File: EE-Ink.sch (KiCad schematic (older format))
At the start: 14 parts

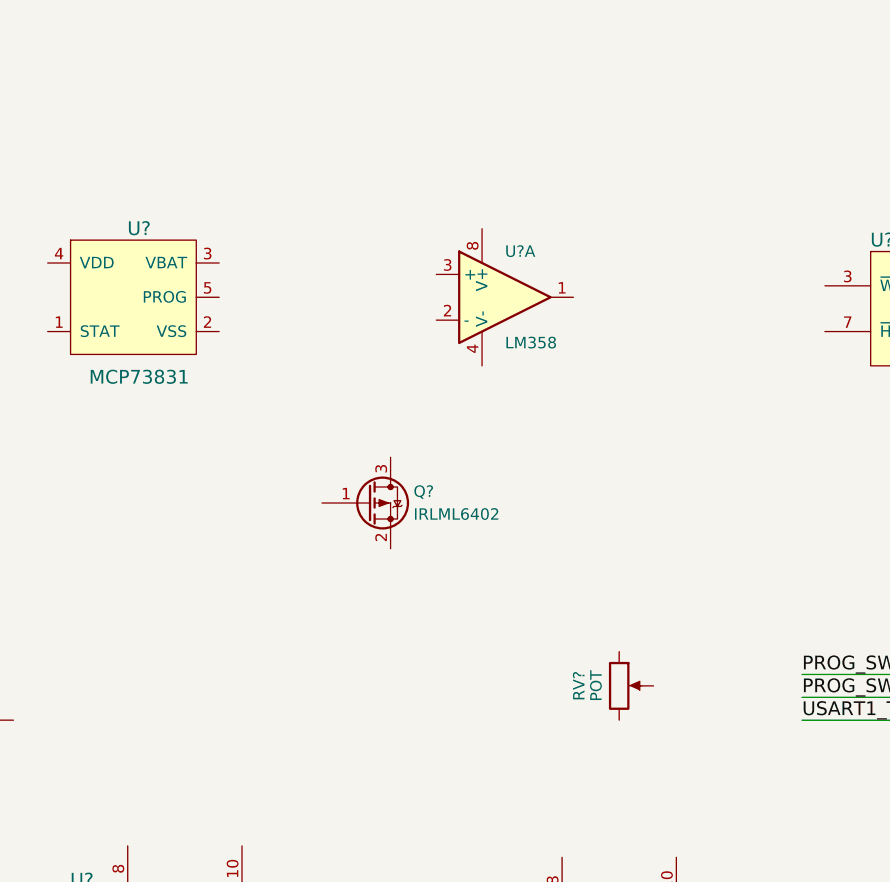
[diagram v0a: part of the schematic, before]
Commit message: Connected op-amp.
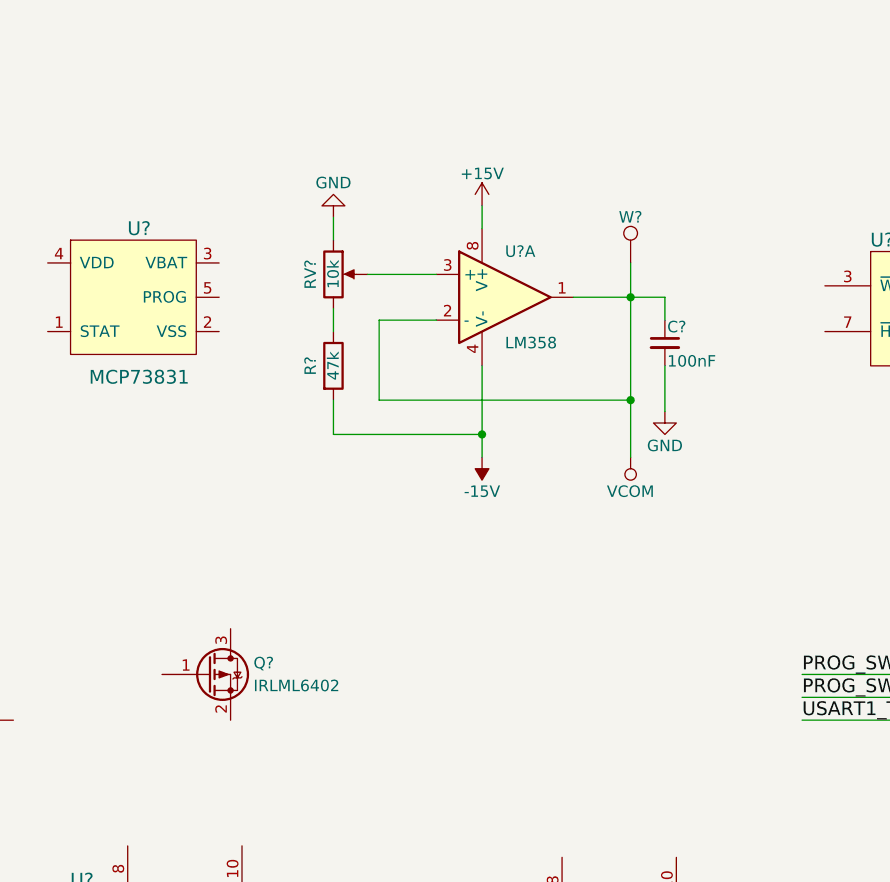
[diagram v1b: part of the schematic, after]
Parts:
- added C?: 100nF, symbol C_Small
- added R?: 47k, symbol R
- added W?: TEST_1P, symbol TEST_1P
- RV?: value POT -> 10k
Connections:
- net +15V: now also U?.8 (V+)
- net -15V: now also U?.4 (V-), R?.2
- net GND: now also RV?.1, C?.2
- net VCOM: now also U?.1, U?.2 (-), C?.1, W?.1
- net at U?.3 (+): now also RV?.2
- net at RV?.3: now also R?.1
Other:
- moved on the sheet: Q?, RV?
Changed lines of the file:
@@
 L Q_PMOS_GSD Q?
 U 1 1 58D82351
-P 7100 3350
-F 0 "Q?" H 7300 3400 50  0000 L CNN
-F 1 "IRLML6402" H 7300 3300 50  0000 L CNN
-F 2 "" H 7300 3450 50  0001 C CNN
-F 3 "" H 7100 3350 50  0001 C CNN
-	1    7100 3350
+P 6400 4100
+F 0 "Q?" H 6600 4150 50  0000 L CNN
+F 1 "IRLML6402" H 6600 4050 50  0000 L CNN
+F 2 "" H 6600 4200 50  0001 C CNN
+F 3 "" H 6400 4100 50  0001 C CNN
+	1    6400 4100
 	1    0    0    -1
 $EndComp
@@
 L POT RV?
 U 1 1 58D82C23
-P 8200 4150
-F 0 "RV?" V 8025 4150 50  0000 C CNN
-F 1 "POT" V 8100 4150 50  0000 C CNN
-F 2 "" H 8200 4150 50  0001 C CNN
-F 3 "" H 8200 4150 50  0001 C CNN
-	1    8200 4150
+P 6950 2350
+F 0 "RV?" V 6850 2350 50  0000 C CNN
+F 1 "10k" V 6950 2350 50  0000 C CNN
+F 2 "" H 6950 2350 50  0001 C CNN
+F 3 "" H 6950 2350 50  0001 C CNN
+	1    6950 2350
 	1    0    0    -1
 $EndComp
@@
 Text Notes 4250 5800 0    50   ~ 10
 GND?
+$Comp
+L +15V #PWR?
+U 1 1 58D81E59
+P 7600 2050
+F 0 "#PWR?" H 7600 1900 50  0001 C CNN
+F 1 "+15V" H 7600 2190 50  0000 C CNN
+F 2 "" H 7600 2050 50  0001 C CNN
+F 3 "" H 7600 2050 50  0001 C CNN
+	1    7600 2050
+	1    0    0    -1
+$EndComp
+Wire Wire Line
+	7600 2150 7600 2050
+Wire Wire Line
+	7400 2350 7100 2350
+$Comp
+L R R?
+U 1 1 58D8389F
+P 6950 2750
+F 0 "R?" V 6850 2750 50  0000 C CNN
+F 1 "47k" V 6950 2750 50  0000 C CNN
+F 2 "" V 6880 2750 50  0001 C CNN
+F 3 "" H 6950 2750 50  0001 C CNN
+	1    6950 2750
+	1    0    0    -1
+$EndComp
+$Comp
+L -15V #PWR?
+U 1 1 58D84B60
+P 7600 3150
+F 0 "#PWR?" H 7600 3250 50  0001 C CNN
+F 1 "-15V" H 7600 3300 50  0000 C CNN
+F 2 "" H 7600 3150 50  0001 C CNN
+F 3 "" H 7600 3150 50  0001 C CNN
+	1    7600 3150
+	-1   0    0    1
+$EndComp
+Wire Wire Line
+	6950 2600 6950 2500
+Wire Wire Line
+	7600 2750 7600 3150
+Wire Wire Line
+	6950 2900 6950 3050
+Wire Wire Line
+	6950 3050 7600 3050
+Connection ~ 7600 3050
+$Comp
+L VCOM #PWR?
+U 1 1 58D8898E
+P 8250 3150
+F 0 "#PWR?" H 8250 3000 50  0001 C CNN
+F 1 "VCOM" H 8250 3300 50  0000 C CNN
+F 2 "" H 8250 3150 50  0001 C CNN
+F 3 "" H 8250 3150 50  0001 C CNN
+	1    8250 3150
+	-1   0    0    1
+$EndComp
+$Comp
+L TEST_1P W?
+U 1 1 58D8AC37
+P 8250 2300
+F 0 "W?" H 8250 2500 50  0000 C CNN
+F 1 "TEST_1P" H 8250 2500 50  0001 C CNN
+F 2 "" H 8450 2300 50  0001 C CNN
+F 3 "" H 8450 2300 50  0001 C CNN
+	1    8250 2300
+	1    0    0    -1
+$EndComp
+Wire Wire Line
+	8250 3150 8250 2300
+Wire Wire Line
+	8000 2450 8400 2450
+Connection ~ 8250 2450
+Wire Wire Line
+	7400 2550 7150 2550
+Wire Wire Line
+	7150 2550 7150 2900
+Wire Wire Line
+	7150 2900 8250 2900
+Connection ~ 8250 2900
+$Comp
+L GND #PWR?
+U 1 1 58D8AEED
+P 6950 2100
+F 0 "#PWR?" H 6950 1850 50  0001 C CNN
+F 1 "GND" H 6950 1950 50  0000 C CNN
+F 2 "" H 6950 2100 50  0001 C CNN
+F 3 "" H 6950 2100 50  0001 C CNN
+	1    6950 2100
+	-1   0    0    1
+$EndComp
+Wire Wire Line
+	6950 2200 6950 2100
+$Comp
+L C_Small C?
+U 1 1 58D8D33B
+P 8400 2650
+F 0 "C?" H 8410 2720 50  0000 L CNN
+F 1 "100nF" H 8410 2570 50  0000 L CNN
+F 2 "" H 8400 2650 50  0001 C CNN
+F 3 "" H 8400 2650 50  0001 C CNN
+	1    8400 2650
+	1    0    0    -1
+$EndComp
+Wire Wire Line
+	8400 2450 8400 2550
+$Comp
+L GND #PWR?
+U 1 1 58D8DBDF
+P 8400 2950
+F 0 "#PWR?" H 8400 2700 50  0001 C CNN
+F 1 "GND" H 8400 2800 50  0000 C CNN
+F 2 "" H 8400 2950 50  0001 C CNN
+F 3 "" H 8400 2950 50  0001 C CNN
+	1    8400 2950
+	1    0    0    -1
+$EndComp
+Wire Wire Line
+	8400 2950 8400 2750
 $EndSCHEMATC

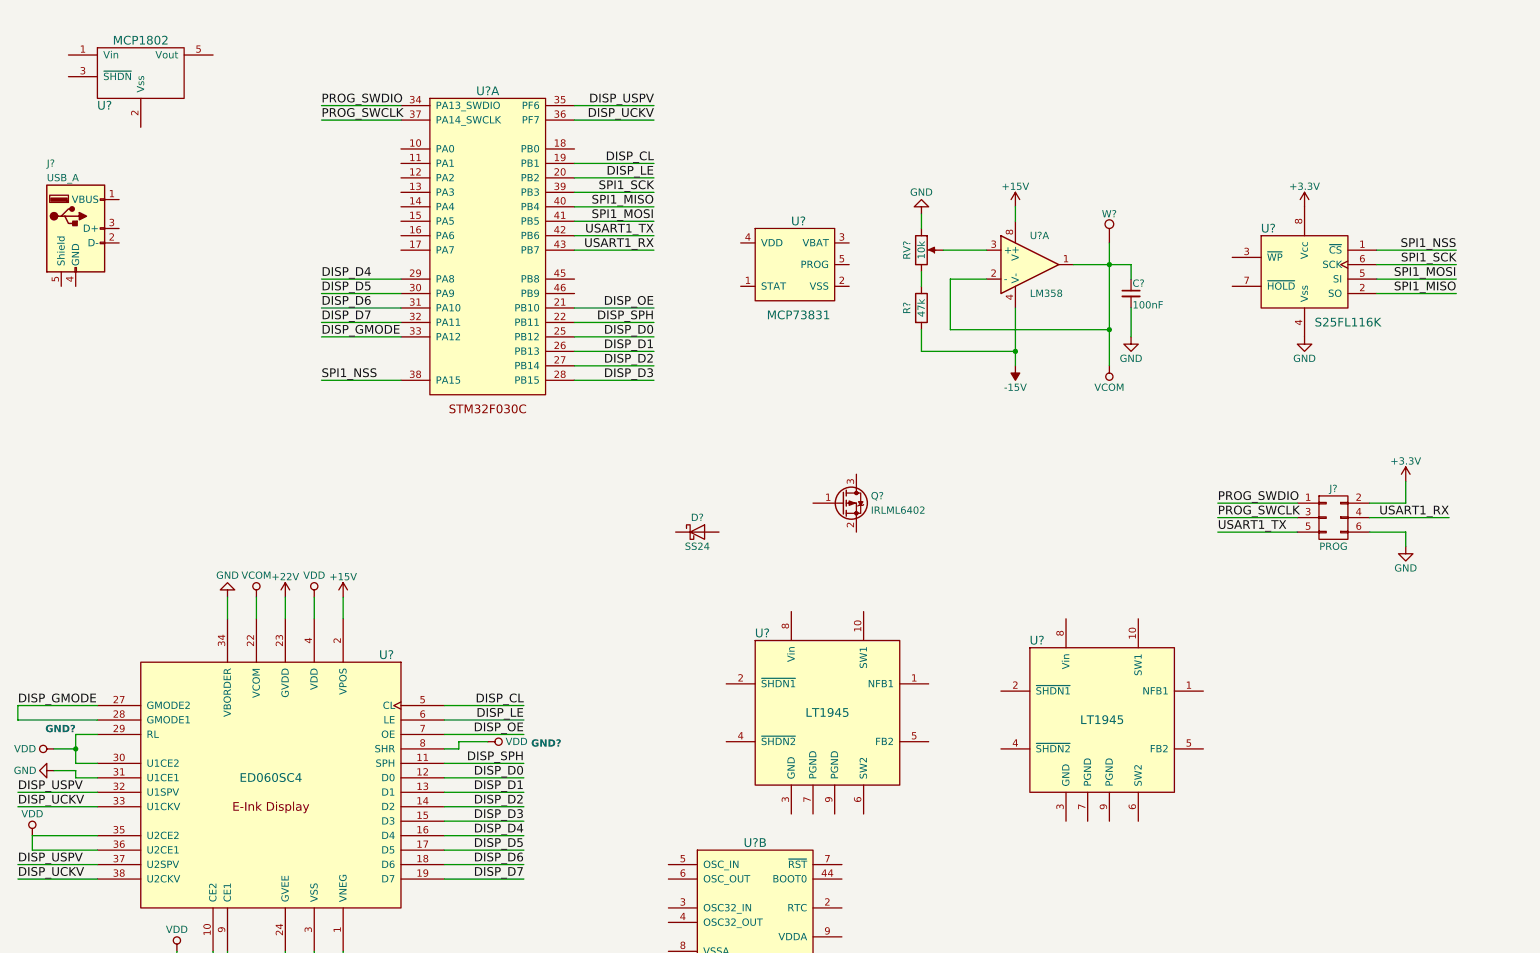
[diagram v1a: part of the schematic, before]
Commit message: Added ftdi chip and started wiring power circuitry.
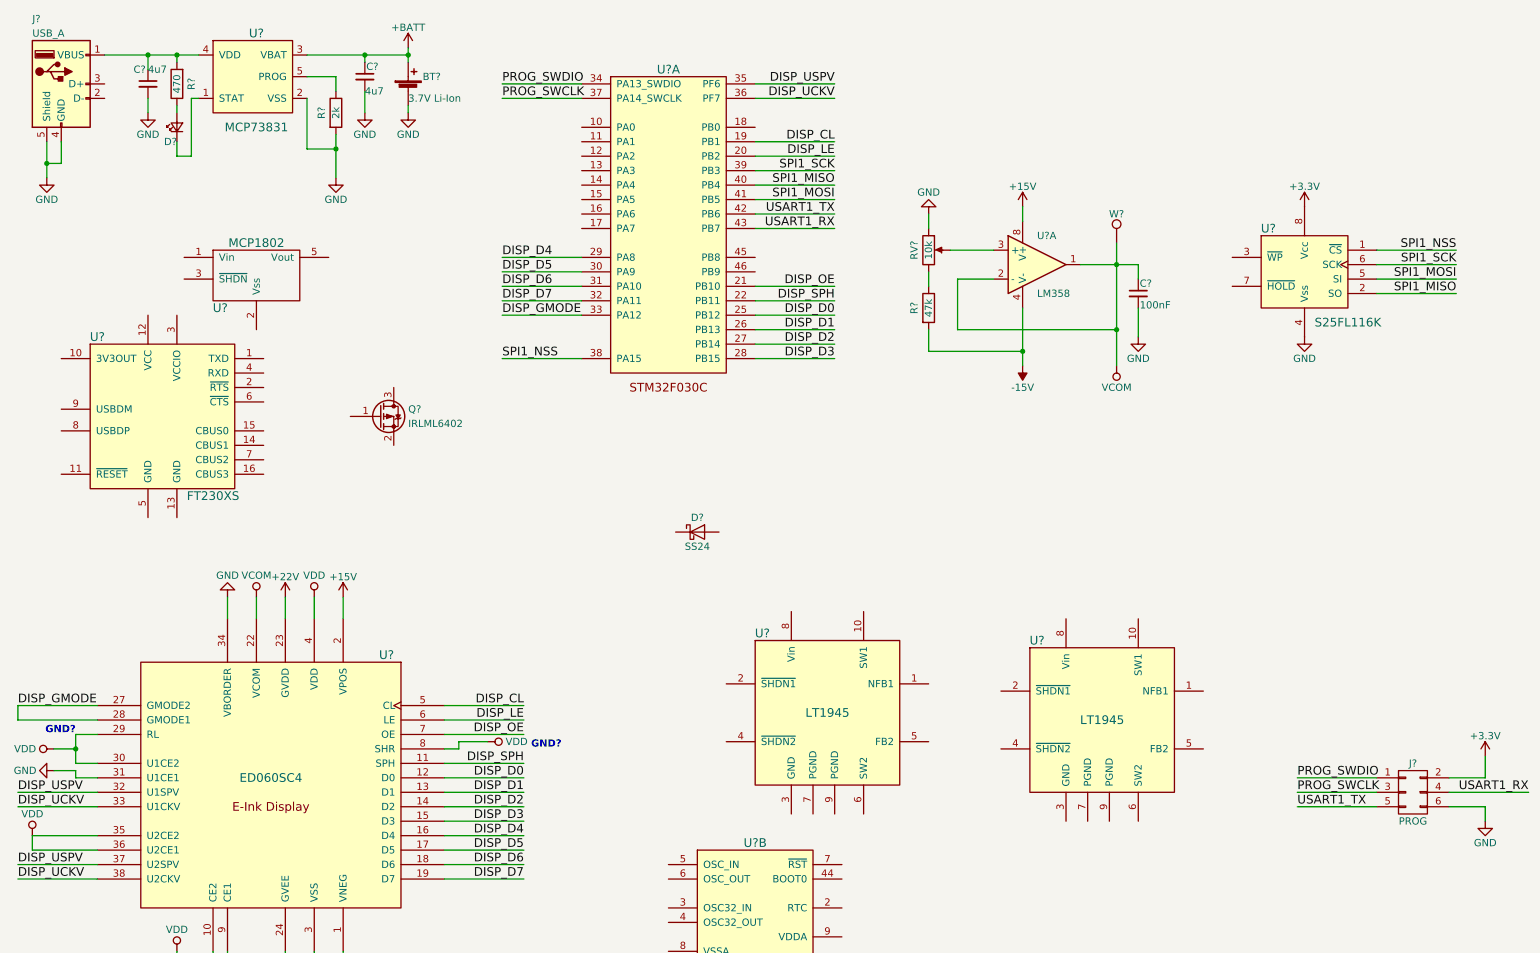
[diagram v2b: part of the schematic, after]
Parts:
- added BT?: 3.7V Li-Ion, symbol Battery_Cell
- added C? (x2): 4u7, symbol C_Small
- added D?: LED_Small, symbol LED_Small
- added R?: 470, symbol R
- added R?: 2k, symbol R
- added U?: FT230XS, symbol FT230XS
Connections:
- net GND: now also J?.4 (GND), J?.5 (Shield), U?.2 (VSS), BT?.2 (-), C?.2, C?.2, R?.2
- net at U?.1 (STAT): now also D?.1 (K)
- net +BATT: now reaches U?.3 (VBAT)
- net +BATT: now also BT?.1 (+), C?.1
- net at U?.4 (VDD): now also J?.1 (VBUS), C?.1, R?.2
- net at U?.5 (PROG): now also R?.1
- new net: D?.2 (A), R?.1
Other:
- moved on the sheet: C?, J?, Q?, R?, RV?, U?, U?A, W?

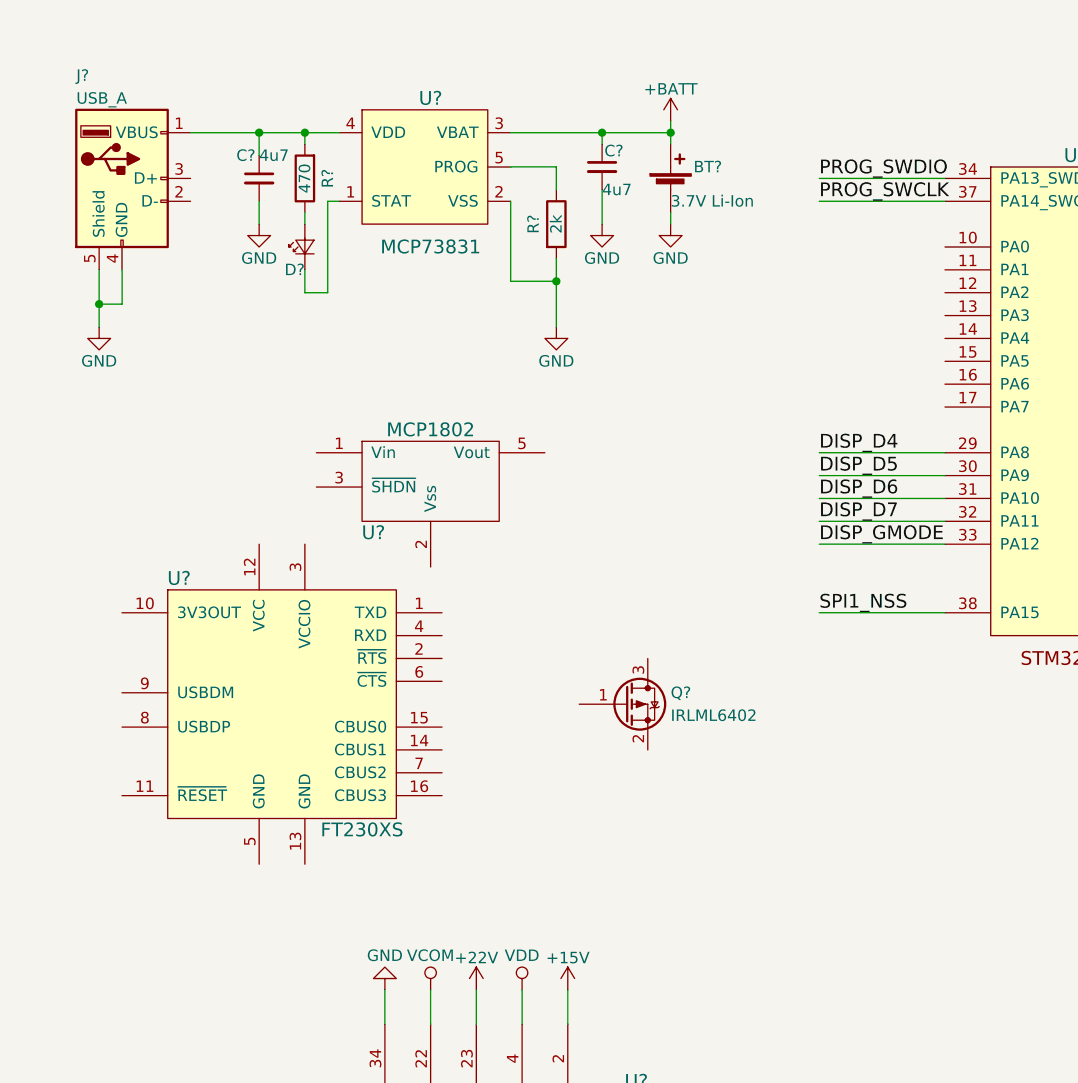
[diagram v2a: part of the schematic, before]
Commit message: Wired up the FTDI and charging circuit.
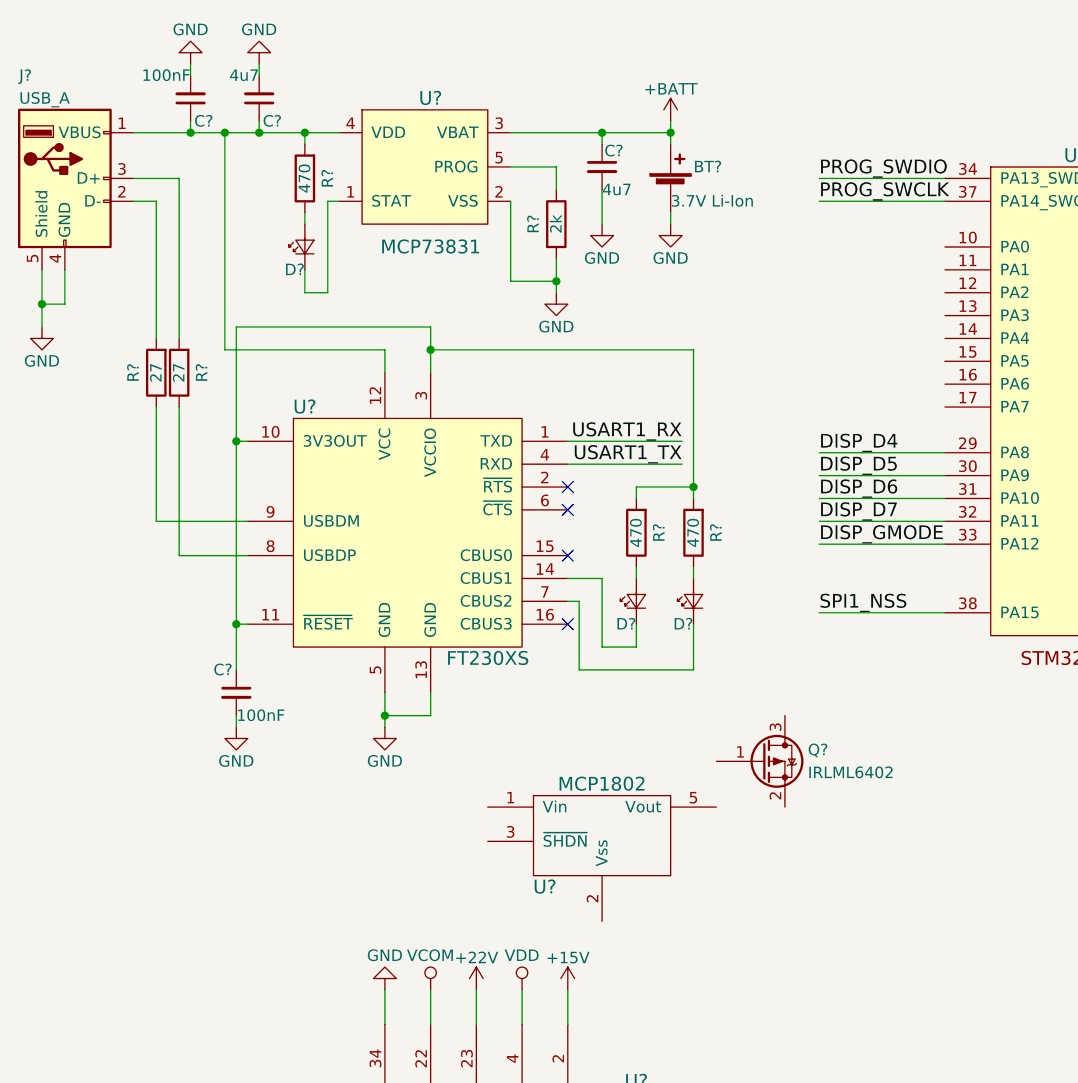
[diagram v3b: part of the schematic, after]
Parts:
- removed C?: 4u7, symbol C_Small
- added C? (x2): 100nF, symbol C_Small
- added C?: 4u7, symbol C_Small
- added D? (x2): LED_Small, symbol LED_Small
- added R? (x2): 470, symbol R
- added R? (x2): 27, symbol R
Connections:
- net GND: now also U?.13 (GND), U?.5 (GND), C?.2, C?.2, C?.2
- net USART1_RX: now also U?.1 (TXD)
- net USART1_TX: now also U?.4 (RXD)
- net at J?.1 (VBUS), R?.2, U?.4 (VDD): now also U?.12 (VCC), C?.1, C?.1
- net at J?.2 (D-): now also R?.2
- net at J?.3 (D+): now also R?.2
- net at U?.10 (3V3OUT): now also U?.11 (~RESET), U?.3 (VCCIO), C?.1, R?.2, R?.2
- net at U?.14 (CBUS1): now also D?.1 (K)
- net at U?.7 (CBUS2): now also D?.1 (K)
- net at U?.8 (USBDP): now also R?.1
- net at U?.9 (USBDM): now also R?.1
- new net: D?.2 (A), R?.1 (x2)
- no-connect marks 0 -> 4
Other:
- moved on the sheet: J?, Q?, U?
